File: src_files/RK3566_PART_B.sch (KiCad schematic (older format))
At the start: 2 parts, among them U1 RK3566

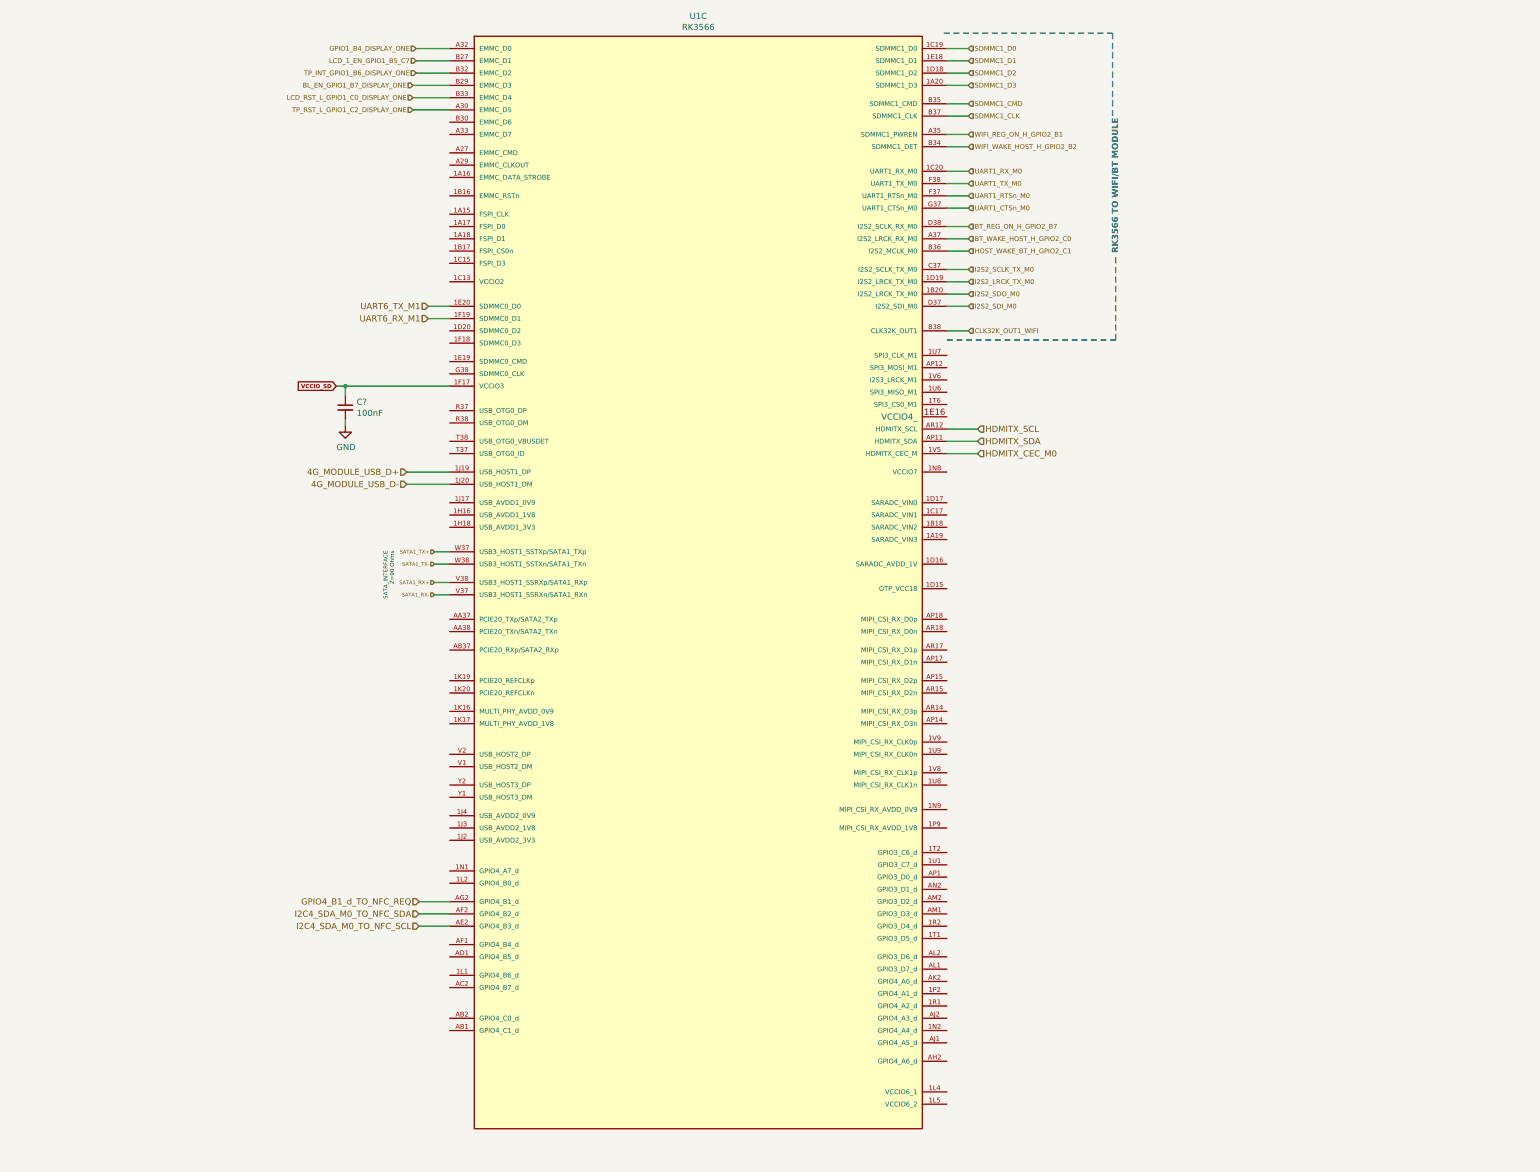
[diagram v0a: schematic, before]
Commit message: schematic capture complete
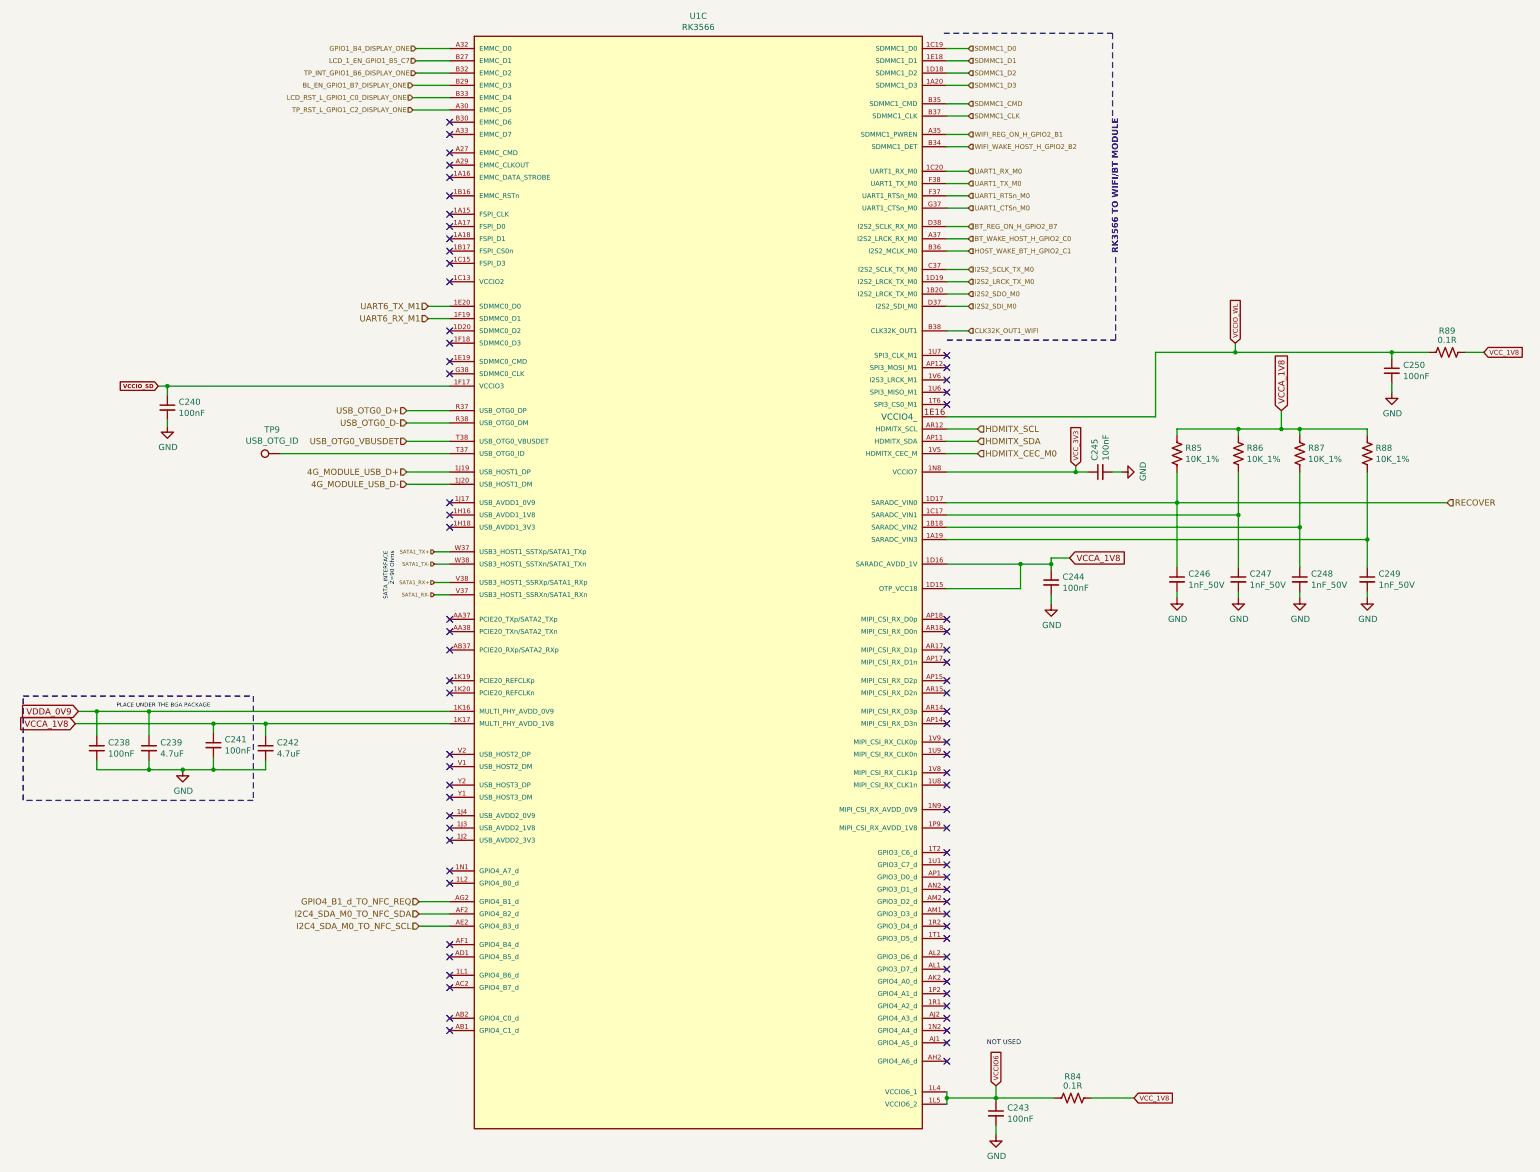
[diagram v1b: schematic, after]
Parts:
- added C238, C241, C243, C244, C245, C250: 100nF, Capacitor_SMD:C_0402_1005Metric, symbol Device:C_Small
- added C239, C242: 4.7uF, Capacitor_SMD:C_0402_1005Metric, symbol Device:C_Small
- added C246, C247, C248, C249: 1nF_50V, Capacitor_SMD:C_0402_1005Metric, symbol Device:C_Small
- added R84, R89: 0.1R, Resistor_SMD:R_0402_1005Metric, symbol Device:R_US
- added R85, R86, R87, R88: 10K_1%, Resistor_SMD:R_0402_1005Metric, symbol Device:R_US
- added TP9: USB_OTG_ID, TestPoint:TestPoint_Pad_D1.0mm, symbol Connector:TestPoint
- C240: renamed from C?; footprint (none) -> Capacitor_SMD:C_0402_1005Metric
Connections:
- net GND: now also C238.2, C239.2, C241.2, C242.2, C243.2, C244.2, C245.2, C246.2, C247.2, C248.2, C249.2, C250.2
- net at U1.1A19 (SARADC_VIN3): now also C249.1, R88.2
- net at U1.1B18 (SARADC_VIN2): now also C248.1, R87.2
- net at U1.1C17 (SARADC_VIN1): now also C247.1, R86.2
- net VCCA_1V8: now reaches U1.1D15 (OTP_VCC18)
- net VCCA_1V8: now also U1.1D16 (SARADC_AVDD_1V), U1.1K17 (MULTI_PHY_AVDD_1V8), C241.1, C242.1, C244.1, R85.1, R86.1, R87.1, R88.1
- net RECOVER: now reaches U1.1D17 (SARADC_VIN0)
- net RECOVER: now also C246.1, R85.2
- net VCCIO_WL: now reaches U1.1E16 (VCCIO4_)
- net VCCIO_WL: now also C250.1, R89.2
- net VDDA_0V9: now reaches U1.1K16 (MULTI_PHY_AVDD_0V9)
- net VDDA_0V9: now also C238.1, C239.1
- net VCCIO6: now reaches U1.1L4 (VCCIO6_1)
- net VCCIO6: now also U1.1L5 (VCCIO6_2), C243.1, R84.2
- net VCC_3V3: now reaches U1.1N8 (VCCIO7)
- net VCC_3V3: now also C245.1
- net USB_OTG0_D+: now reaches U1.R37 (USB_OTG0_DP)
- net USB_OTG0_D-: now reaches U1.R38 (USB_OTG0_DM)
- net at U1.T37 (USB_OTG0_ID): now also TP9.1
- net USB_OTG0_VBUSDET: now reaches U1.T38 (USB_OTG0_VBUSDET)
- new net VCC_1V8: R84.1, R89.1
- no-connect marks 0 -> 75
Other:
- note added: "NOT USED"
- note added: "PLACE UNDER THE BGA PACKAGE\n"
- moved on the sheet: C240

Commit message: updated footprint and schematics
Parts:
- U1: footprint greencharge-footprints:BGA828C65P31X31_2100X2100X161N -> greencharge-footprints:RK366_BGA-565_20x18_15.5x14.4mm
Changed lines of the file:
@@
 $Descr A3 16535 11693
 encoding utf-8
-Sheet 12 15
+Sheet 11 16
 Title ""
 Date ""
@@
 F 0 "U1" H 6050 240 50  0000 C CNN
 F 1 "RK3566" H 6050 149 50  0000 C CNN
-F 2 "greencharge-footprints:BGA828C65P31X31_2100X2100X161N" H 5475 475 50  0001 C CNN
+F 2 "greencharge-footprints:RK366_BGA-565_20x18_15.5x14.4mm" H 5475 475 50  0001 C CNN
 F 3 "" H 5475 475 50  0001 C CNN
 	3    6025 575

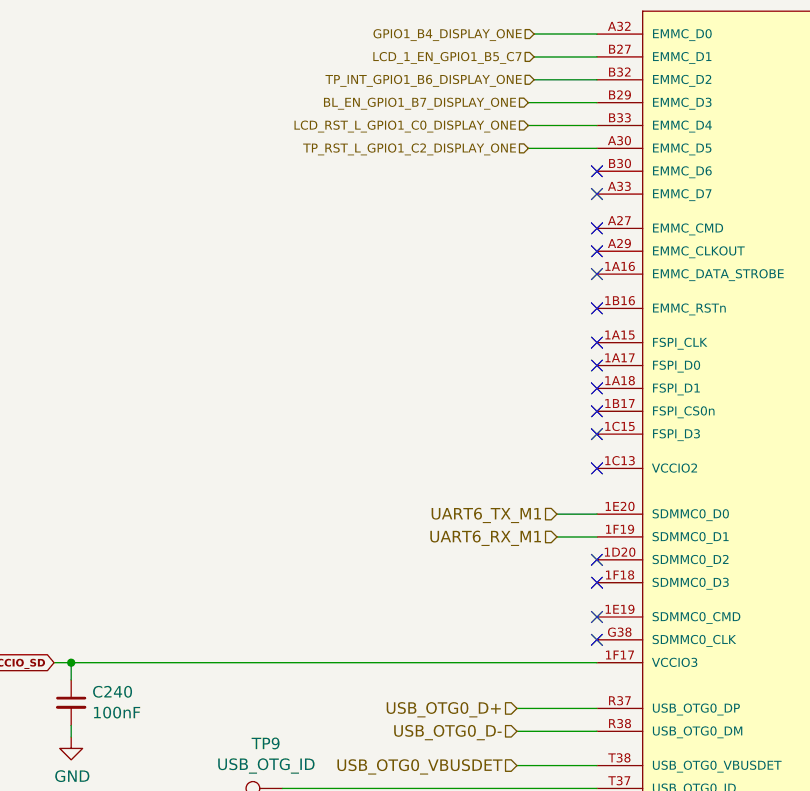
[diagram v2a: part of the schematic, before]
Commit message: update 1 extra hdmi to mipi interface
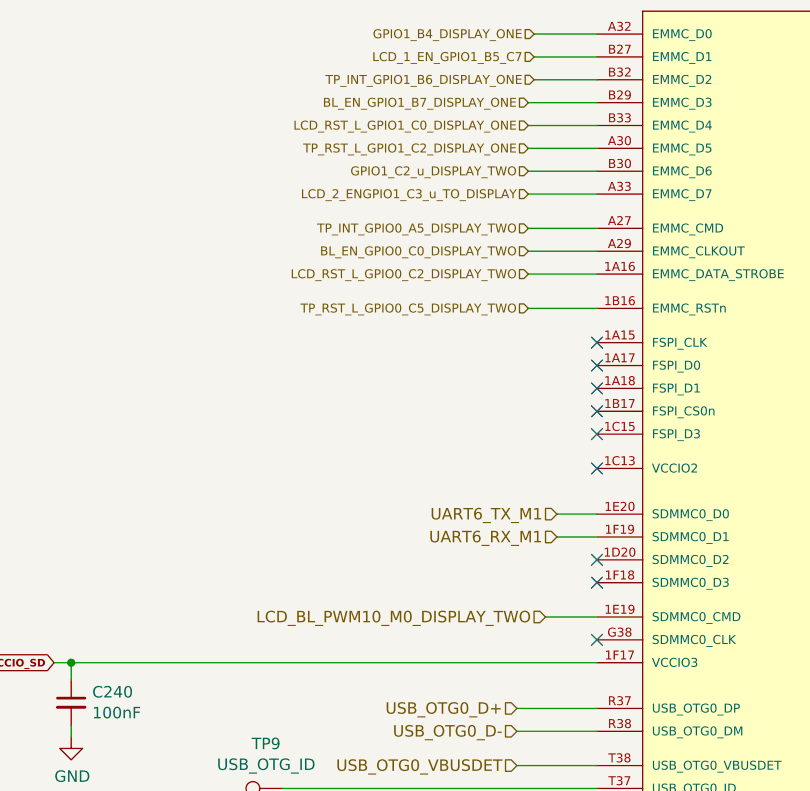
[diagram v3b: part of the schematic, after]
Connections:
- net LCD_RST_L_GPIO0_C2_DISPLAY_TWO: now reaches U1.1A16 (EMMC_DATA_STROBE)
- net TP_RST_L_GPIO0_C5_DISPLAY_TWO: now reaches U1.1B16 (EMMC_RSTn)
- net LCD_BL_PWM10_M0_DISPLAY_TWO: now reaches U1.1E19 (SDMMC0_CMD)
- net TP_INT_GPIO0_A5_DISPLAY_TWO: now reaches U1.A27 (EMMC_CMD)
- net BL_EN_GPIO0_C0_DISPLAY_TWO: now reaches U1.A29 (EMMC_CLKOUT)
- net LCD_2_ENGPIO1_C3_u_TO_DISPLAY: now reaches U1.A33 (EMMC_D7)
- net GPIO1_C2_u_DISPLAY_TWO: now reaches U1.B30 (EMMC_D6)
- no-connect marks 75 -> 68
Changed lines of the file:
@@
 $Descr A3 16535 11693
 encoding utf-8
-Sheet 11 16
+Sheet 12 15
 Title ""
 Date ""
@@
 Wire Wire Line
 	10425 3650 11700 3650
-NoConn ~ 4025 1775
-NoConn ~ 4025 1875
-NoConn ~ 4025 2025
-NoConn ~ 4025 2125
 $Comp
 L GCL_Integrated-Circuits:RK3566 U?
@@
 	1    0    0    -1
 $EndComp
-NoConn ~ 4025 2225
-NoConn ~ 4025 2375
 NoConn ~ 4025 2525
 NoConn ~ 4025 2625
@@
 NoConn ~ 4025 3475
 NoConn ~ 4025 3575
-NoConn ~ 4025 3725
 NoConn ~ 4025 3825
 NoConn ~ 4025 4875
@@
 Text Notes 8400 9300 0    39   ~ 0
 NOT USED
+Text HLabel 3725 1775 0    39   Input ~ 0
+GPIO1_C2_u_DISPLAY_TWO
+Wire Wire Line
+	4025 1775 3725 1775
+Text HLabel 3725 1875 0    39   Input ~ 0
+LCD_2_ENGPIO1_C3_u_TO_DISPLAY
+Wire Wire Line
+	4025 1875 3725 1875
+Text HLabel 3725 2025 0    39   Input ~ 0
+TP_INT_GPIO0_A5_DISPLAY_TWO
+Text HLabel 3725 2125 0    39   Input ~ 0
+BL_EN_GPIO0_C0_DISPLAY_TWO
+Text HLabel 3725 2225 0    39   Input ~ 0
+LCD_RST_L_GPIO0_C2_DISPLAY_TWO
+Text HLabel 3725 2375 0    39   Input ~ 0
+TP_RST_L_GPIO0_C5_DISPLAY_TWO
+Wire Wire Line
+	4025 2025 3725 2025
+Wire Wire Line
+	4025 2125 3725 2125
+Wire Wire Line
+	3725 2225 4025 2225
+Wire Wire Line
+	4025 2375 3725 2375
+Text HLabel 3800 3725 0    50   Input ~ 0
+LCD_BL_PWM10_M0_DISPLAY_TWO
+Wire Wire Line
+	4025 3725 3800 3725
 $EndSCHEMATC

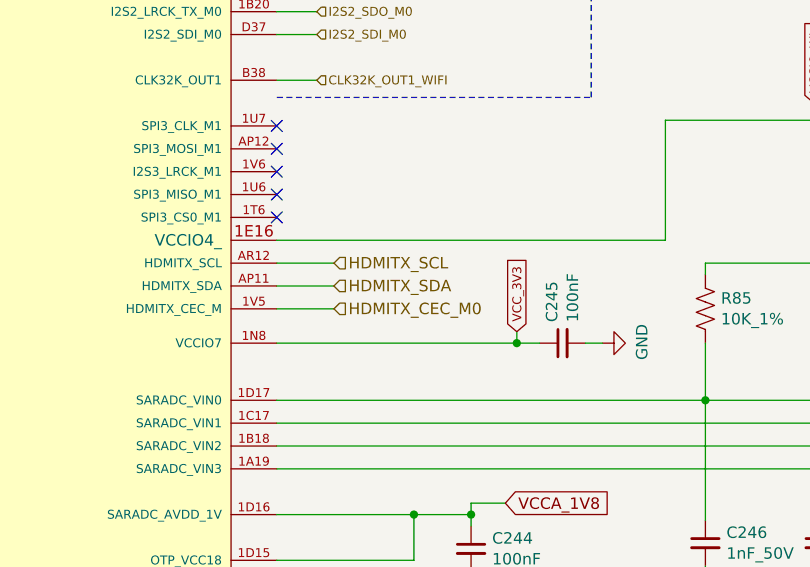
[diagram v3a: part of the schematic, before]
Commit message: complete update on schematic and all display interfaces
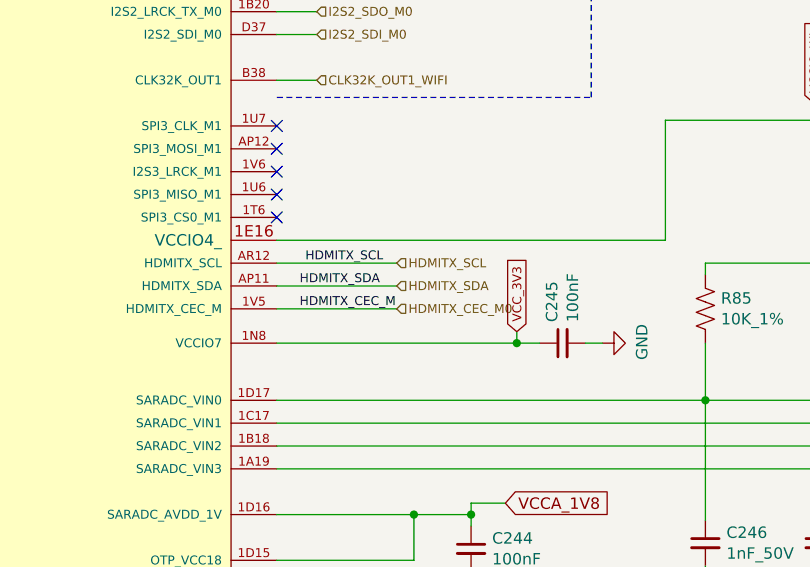
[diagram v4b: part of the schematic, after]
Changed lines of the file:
@@
 $Descr A3 16535 11693
 encoding utf-8
-Sheet 12 15
+Sheet 9 15
 Title ""
 Date ""
@@
 Wire Wire Line
 	3725 1675 4025 1675
-Text HLabel 8325 4475 2    50   Input ~ 0
-HDMITX_CEC_M0
-Wire Wire Line
-	8075 4475 8325 4475
-Text HLabel 8325 4375 2    50   Input ~ 0
-HDMITX_SDA
-Text HLabel 8325 4275 2    50   Input ~ 0
-HDMITX_SCL
-Wire Wire Line
-	8075 4275 8325 4275
-Wire Wire Line
-	8075 4375 8325 4375
 Text HLabel 3675 4625 0    50   Input ~ 0
 4G_MODULE_USB_D+
@@
 Wire Wire Line
 	4025 3725 3800 3725
+Text Label 8175 4475 0    39   ~ 0
+HDMITX_CEC_M
+Text Label 8175 4375 0    39   ~ 0
+HDMITX_SDA
+Text Label 8200 4275 0    39   ~ 0
+HDMITX_SCL
+Wire Wire Line
+	8075 4375 8600 4375
+Wire Wire Line
+	8075 4275 8600 4275
+Wire Wire Line
+	8075 4475 8600 4475
+Text HLabel 8600 4275 2    39   Input ~ 0
+HDMITX_SCL
+Text HLabel 8600 4375 2    39   Input ~ 0
+HDMITX_SDA
+Text HLabel 8600 4475 2    39   Input ~ 0
+HDMITX_CEC_M0
 $EndSCHEMATC

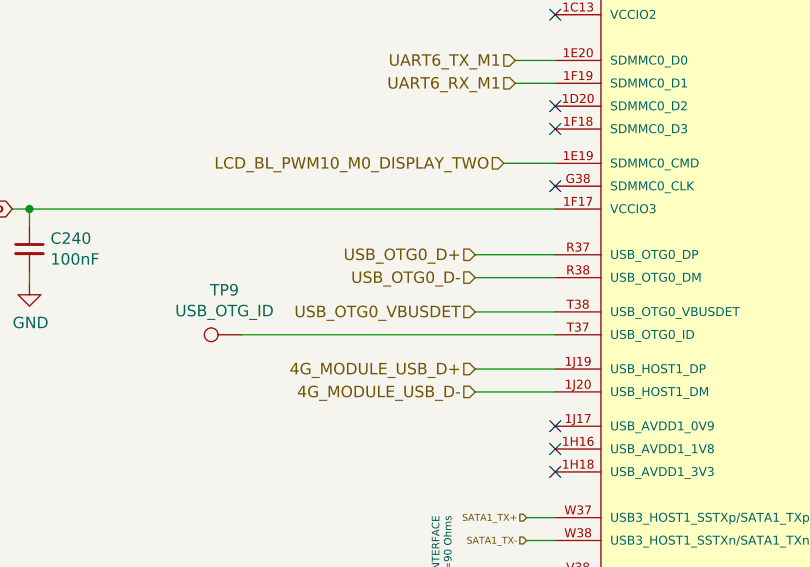
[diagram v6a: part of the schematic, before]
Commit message: updates rules check and associations
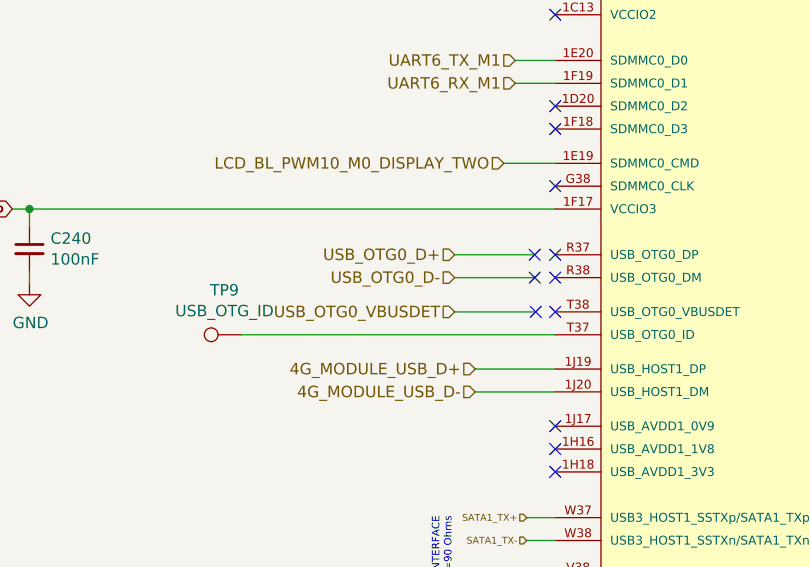
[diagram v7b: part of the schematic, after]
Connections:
- net USB_OTG0_D+: no longer U1.R37 (USB_OTG0_DP)
- net USB_OTG0_D-: no longer U1.R38 (USB_OTG0_DM)
- net USB_OTG0_VBUSDET: no longer U1.T38 (USB_OTG0_VBUSDET)
- no-connect marks 68 -> 74
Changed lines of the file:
@@
 Wire Wire Line
 	4025 8125 3775 8125
-Text HLabel 3675 4375 0    50   Input ~ 0
+Text HLabel 3585 4375 0    50   Input ~ 0
 USB_OTG0_VBUSDET
 $Comp
@@
 	4025 4475 2650 4475
 Wire Wire Line
-	4025 4375 3675 4375
-Text HLabel 3675 4225 0    50   Input ~ 0
+	3935 4375 3585 4375
+Text HLabel 3585 4225 0    50   Input ~ 0
 USB_OTG0_D-
-Text HLabel 3675 4125 0    50   Input ~ 0
+Text HLabel 3585 4125 0    50   Input ~ 0
 USB_OTG0_D+
 Wire Wire Line
-	4025 4125 3675 4125
-Wire Wire Line
-	3675 4225 4025 4225
+	3935 4125 3585 4125
+Wire Wire Line
+	3585 4225 3935 4225
 Text HLabel 12150 4875 2    50   Input ~ 0
 RECOVER
@@
 Text HLabel 8600 4475 2    39   Input ~ 0
 HDMITX_CEC_M0
+NoConn ~ 3935 4125
+NoConn ~ 3935 4225
+NoConn ~ 3940 4375
+NoConn ~ 4025 4375
+NoConn ~ 4025 4225
+NoConn ~ 4025 4125
 $EndSCHEMATC
